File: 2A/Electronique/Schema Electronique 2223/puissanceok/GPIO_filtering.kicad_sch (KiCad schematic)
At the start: 4 parts, among them J201 Conn_01x02

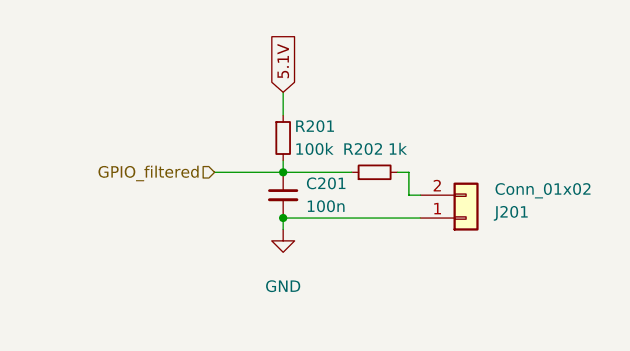
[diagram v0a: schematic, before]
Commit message: update schematic
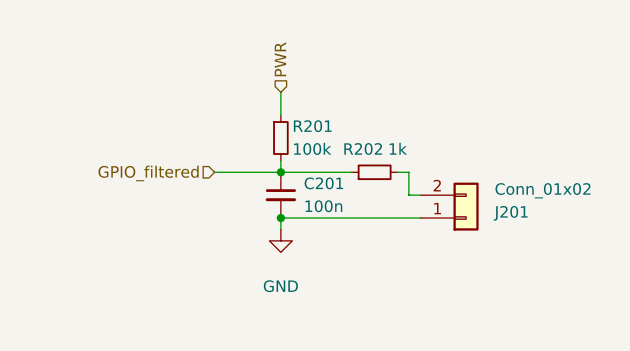
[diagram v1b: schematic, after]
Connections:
- net 5.1V renamed PWR
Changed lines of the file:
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@@
 (kicad_sch (version 20230121) (generator eeschema)
   (paper "A4")
-  (junction (at 122.174 81.28) (diameter 0) (color 0 0 0 0)
-  )
-  (junction (at 122.174 86.36) (diameter 0) (color 0 0 0 0)
-  )
-  (wire (pts (xy 122.174 87.63) (xy 122.174 86.36))
+  (junction (at 121.92 81.28) (diameter 0) (color 0 0 0 0)
+  )
+  (junction (at 121.92 86.36) (diameter 0) (color 0 0 0 0)
+  )
+  (wire (pts (xy 121.92 87.63) (xy 121.92 86.36))
+    (stroke (width 0) (type default))
+  )
+  (wire (pts (xy 121.92 72.39) (xy 121.92 74.93))
     (stroke (width 0) (type default))
   )
@@
     (stroke (width 0) (type default))
   )
-  (wire (pts (xy 122.174 72.39) (xy 122.174 74.93))
-    (stroke (width 0) (type default))
-  )
   (wire (pts (xy 136.144 83.82) (xy 137.414 83.82))
     (stroke (width 0) (type default))
   )
-  (wire (pts (xy 122.174 81.28) (xy 114.554 81.28))
+  (wire (pts (xy 121.92 80.01) (xy 121.92 81.28))
+    (stroke (width 0) (type default))
+  )
+  (wire (pts (xy 121.92 81.28) (xy 129.794 81.28))
     (stroke (width 0) (type default))
   )
@@
     (stroke (width 0) (type default))
   )
-  (wire (pts (xy 122.174 80.01) (xy 122.174 81.28))
-    (stroke (width 0) (type default))
-  )
-  (wire (pts (xy 137.414 86.36) (xy 122.174 86.36))
-    (stroke (width 0) (type default))
-  )
-  (wire (pts (xy 122.174 81.28) (xy 129.794 81.28))
-    (stroke (width 0) (type default))
-  )
-  (global_label "5.1V" (shape input) (at 122.174 72.39 90) (fields_autoplaced)
+  (wire (pts (xy 121.92 86.36) (xy 137.414 86.36))
+    (stroke (width 0) (type default))
+  )
+  (wire (pts (xy 114.554 81.28) (xy 121.92 81.28))
+    (stroke (width 0) (type default))
+  )
+  (hierarchical_label "PWR" (shape input) (at 121.92 72.39 90) (fields_autoplaced)
     (effects (font (size 1.27 1.27)) (justify left))
-    (property "Intersheetrefs" "${INTERSHEET_REFS}" (at 122.174 65.2924 90)
-      (effects (font (size 1.27 1.27)) (justify left) hide)
-    )
   )
   (hierarchical_label "GPIO_filtered" (shape input) (at 114.554 81.28 180) (fields_autoplaced)
     (effects (font (size 1.27 1.27)) (justify right))
   )
-  (symbol (lib_id "Device:R_Small") (at 122.174 77.47 0) (unit 1)
+  (symbol (lib_id "Device:R_Small") (at 121.92 77.47 0) (unit 1)
     (in_bom yes) (on_board yes) (dnp no)
-    (property "Reference" "R201" (at 123.444 76.2 0)
-      (effects (font (size 1.27 1.27)) (justify left))
-    )
-    (property "Value" "100k" (at 123.444 78.74 0)
-      (effects (font (size 1.27 1.27)) (justify left))
-    )
-    (property "Footprint" "Resistor_SMD:R_0402_1005Metric" (at 122.174 77.47 0)
-      (effects (font (size 1.27 1.27)) hide)
-    )
-    (property "Datasheet" "~" (at 122.174 77.47 0)
+    (property "Reference" "R201" (at 123.19 76.2 0)
+      (effects (font (size 1.27 1.27)) (justify left))
+    )
+    (property "Value" "100k" (at 123.19 78.74 0)
+      (effects (font (size 1.27 1.27)) (justify left))
+    )
+    (property "Footprint" "Resistor_SMD:R_0402_1005Metric" (at 121.92 77.47 0)
+      (effects (font (size 1.27 1.27)) hide)
+    )
+    (property "Datasheet" "~" (at 121.92 77.47 0)
       (effects (font (size 1.27 1.27)) hide)
     )
@@
     )
   )
-  (symbol (lib_id "power:GND") (at 122.174 87.63 0) (unit 1)
+  (symbol (lib_id "power:GND") (at 121.92 87.63 0) (unit 1)
     (in_bom yes) (on_board yes) (dnp no)
-    (property "Reference" "#PWR0201" (at 122.174 93.98 0)
-      (effects (font (size 1.27 1.27)) hide)
-    )
-    (property "Value" "GND" (at 122.174 93.98 0)
+    (property "Reference" "#PWR0201" (at 121.92 93.98 0)
+      (effects (font (size 1.27 1.27)) hide)
+    )
+    (property "Value" "GND" (at 121.92 93.98 0)
       (effects (font (size 1.27 1.27)))
     )
-    (property "Footprint" "" (at 122.174 87.63 0)
-      (effects (font (size 1.27 1.27)) hide)
-    )
-    (property "Datasheet" "" (at 122.174 87.63 0)
+    (property "Footprint" "" (at 121.92 87.63 0)
+      (effects (font (size 1.27 1.27)) hide)
+    )
+    (property "Datasheet" "" (at 121.92 87.63 0)
       (effects (font (size 1.27 1.27)) hide)
     )
@@
     )
   )
-  (symbol (lib_id "Device:C_Small") (at 122.174 83.82 0) (unit 1)
+  (symbol (lib_id "Device:C_Small") (at 121.92 83.82 0) (unit 1)
     (in_bom yes) (on_board yes) (dnp no) (fields_autoplaced)
-    (property "Reference" "C201" (at 124.714 82.5563 0)
-      (effects (font (size 1.27 1.27)) (justify left))
-    )
-    (property "Value" "100n" (at 124.714 85.0963 0)
-      (effects (font (size 1.27 1.27)) (justify left))
-    )
-    (property "Footprint" "Capacitor_SMD:C_0402_1005Metric" (at 122.174 83.82 0)
-      (effects (font (size 1.27 1.27)) hide)
-    )
-    (property "Datasheet" "~" (at 122.174 83.82 0)
-      (effects (font (size 1.27 1.27)) hide)
-    )
+    (property "Reference" "C201" (at 124.46 82.5563 0)
+      (effects (font (size 1.27 1.27)) (justify left))
+    )
+    (property "Value" "100n" (at 124.46 85.0963 0)
+      (effects (font (size 1.27 1.27)) (justify left))
+    )
+    (property "Footprint" "Capacitor_SMD:C_0402_1005Metric" (at 121.92 83.82 0)
+      (effects (font (size 1.27 1.27)) hide)
+    )
+    (property "Datasheet" "~" (at 121.92 83.82 0)
+      (effects (font (size 1.27 1.27)) hide)
+    )

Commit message: update schematic
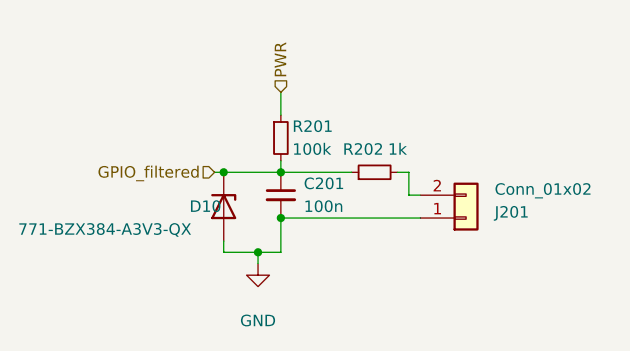
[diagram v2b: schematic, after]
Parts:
- added D10: 771-BZX384-A3V3-QX, Diode_SMD:D_SOD-323, symbol Diode:BZX384xxxx
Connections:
- net GND: now also D10.2 (A)
- net GPIO_filtered: now also D10.1 (K)
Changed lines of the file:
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@@
 (kicad_sch (version 20230121) (generator eeschema)
   (paper "A4")
+  (junction (at 115.57 81.28) (diameter 0) (color 0 0 0 0)
+  )
   (junction (at 121.92 81.28) (diameter 0) (color 0 0 0 0)
   )
   (junction (at 121.92 86.36) (diameter 0) (color 0 0 0 0)
   )
-  (wire (pts (xy 121.92 87.63) (xy 121.92 86.36))
+  (junction (at 119.38 90.17) (diameter 0) (color 0 0 0 0)
+  )
+  (wire (pts (xy 119.38 91.44) (xy 119.38 90.17))
     (stroke (width 0) (type default))
   )
@@
     (stroke (width 0) (type default))
   )
+  (wire (pts (xy 121.92 90.17) (xy 121.92 86.36))
+    (stroke (width 0) (type default))
+  )
   (wire (pts (xy 136.144 83.82) (xy 137.414 83.82))
     (stroke (width 0) (type default))
@@
     (stroke (width 0) (type default))
   )
+  (wire (pts (xy 115.57 81.28) (xy 121.92 81.28))
+    (stroke (width 0) (type default))
+  )
   (wire (pts (xy 121.92 81.28) (xy 129.794 81.28))
     (stroke (width 0) (type default))
@@
     (stroke (width 0) (type default))
   )
+  (wire (pts (xy 119.38 90.17) (xy 121.92 90.17))
+    (stroke (width 0) (type default))
+  )
+  (wire (pts (xy 115.57 88.9) (xy 115.57 90.17))
+    (stroke (width 0) (type default))
+  )
+  (wire (pts (xy 115.57 90.17) (xy 119.38 90.17))
+    (stroke (width 0) (type default))
+  )
   (wire (pts (xy 121.92 86.36) (xy 137.414 86.36))
     (stroke (width 0) (type default))
   )
-  (wire (pts (xy 114.554 81.28) (xy 121.92 81.28))
+  (wire (pts (xy 114.554 81.28) (xy 115.57 81.28))
     (stroke (width 0) (type default))
   )
@@
     )
   )
-  (symbol (lib_id "power:GND") (at 121.92 87.63 0) (unit 1)
-    (in_bom yes) (on_board yes) (dnp no)
-    (property "Reference" "#PWR0201" (at 121.92 93.98 0)
-      (effects (font (size 1.27 1.27)) hide)
-    )
-    (property "Value" "GND" (at 121.92 93.98 0)
+  (symbol (lib_id "Diode:BZX384xxxx") (at 115.57 85.09 270) (unit 1)
+    (in_bom yes) (on_board yes) (dnp no)
+    (property "Reference" "D10" (at 111.76 85.09 90)
+      (effects (font (size 1.27 1.27)) (justify left))
+    )
+    (property "Value" "771-BZX384-A3V3-QX" (at 92.71 87.63 90)
+      (effects (font (size 1.27 1.27)) (justify left))
+    )
+    (property "Footprint" "Diode_SMD:D_SOD-323" (at 111.125 85.09 0)
+      (effects (font (size 1.27 1.27)) hide)
+    )
+    (property "Datasheet" "https://www.mouser.fr/datasheet/2/916/BZX384_Q_SER-2721638.pdf" (at 115.57 85.09 0)
+      (effects (font (size 1.27 1.27)) hide)
+    )
+    (property "Mouser Part Number" "771-BZX384-A3V3-QX" (at 115.57 85.09 90)
+      (effects (font (size 1.27 1.27)) hide)
+    )
+    (pin "2")
+    (pin "1")
+    (instances
+      (project "puissanceok"
+        (path "/50648b18-b1a7-4d76-a5dd-1fad5f3e825e/9b22c488-baa3-42ae-9ef5-b083dc19096a"
+          (reference "D10") (unit 1)
+        )
+        (path "/50648b18-b1a7-4d76-a5dd-1fad5f3e825e/ae22de61-0699-445c-b49e-1232b8ae9dd6"
+          (reference "D11") (unit 1)
+        )
+        (path "/50648b18-b1a7-4d76-a5dd-1fad5f3e825e/991e50e5-567d-4a30-9947-41feef9d79c1"
+          (reference "D12") (unit 1)
+        )
+        (path "/50648b18-b1a7-4d76-a5dd-1fad5f3e825e/461af59c-9ba2-44c6-95d1-ce4131c667f6"
+          (reference "D13") (unit 1)
+        )
+      )
+    )
+  )
+  (symbol (lib_id "power:GND") (at 119.38 91.44 0) (unit 1)
+    (in_bom yes) (on_board yes) (dnp no)
+    (property "Reference" "#PWR0201" (at 119.38 97.79 0)
+      (effects (font (size 1.27 1.27)) hide)
+    )
+    (property "Value" "GND" (at 119.38 97.79 0)
       (effects (font (size 1.27 1.27)))
     )
-    (property "Footprint" "" (at 121.92 87.63 0)
-      (effects (font (size 1.27 1.27)) hide)
-    )
-    (property "Datasheet" "" (at 121.92 87.63 0)
-      (effects (font (size 1.27 1.27)) hide)
-    )
+    (property "Footprint" "" (at 119.38 91.44 0)
+      (effects (font (size 1.27 1.27)) hide)
+    )
+    (property "Datasheet" "" (at 119.38 91.44 0)
+      (effects (font (size 1.27 1.27)) hide)
+    )

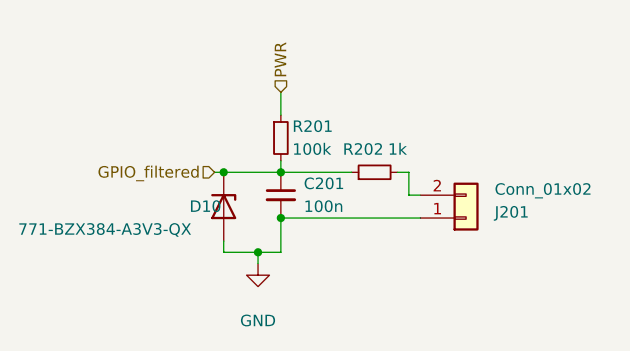
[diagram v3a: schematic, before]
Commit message: suppression diode et changement des feuille hiérarchique
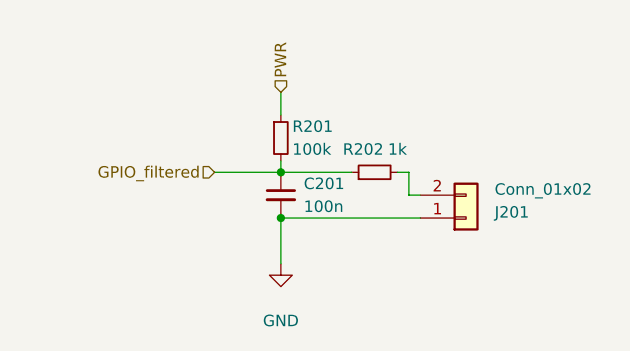
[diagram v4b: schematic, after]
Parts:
- removed D10: 771-BZX384-A3V3-QX, Diode_SMD:D_SOD-323, symbol Diode:BZX384xxxx
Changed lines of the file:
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@@
 (kicad_sch (version 20230121) (generator eeschema)
   (paper "A4")
-  (junction (at 115.57 81.28) (diameter 0) (color 0 0 0 0)
-  )
   (junction (at 121.92 81.28) (diameter 0) (color 0 0 0 0)
   )
   (junction (at 121.92 86.36) (diameter 0) (color 0 0 0 0)
-  )
-  (junction (at 119.38 90.17) (diameter 0) (color 0 0 0 0)
-  )
-  (wire (pts (xy 119.38 91.44) (xy 119.38 90.17))
-    (stroke (width 0) (type default))
   )
   (wire (pts (xy 121.92 72.39) (xy 121.92 74.93))
@@
     (stroke (width 0) (type default))
   )
-  (wire (pts (xy 121.92 90.17) (xy 121.92 86.36))
+  (wire (pts (xy 121.92 86.36) (xy 121.92 91.44))
     (stroke (width 0) (type default))
   )
@@
     (stroke (width 0) (type default))
   )
-  (wire (pts (xy 115.57 81.28) (xy 121.92 81.28))
+  (wire (pts (xy 114.554 81.28) (xy 121.92 81.28))
     (stroke (width 0) (type default))
   )
@@
     (stroke (width 0) (type default))
   )
-  (wire (pts (xy 119.38 90.17) (xy 121.92 90.17))
-    (stroke (width 0) (type default))
-  )
-  (wire (pts (xy 115.57 88.9) (xy 115.57 90.17))
-    (stroke (width 0) (type default))
-  )
-  (wire (pts (xy 115.57 90.17) (xy 119.38 90.17))
-    (stroke (width 0) (type default))
-  )
   (wire (pts (xy 121.92 86.36) (xy 137.414 86.36))
-    (stroke (width 0) (type default))
-  )
-  (wire (pts (xy 114.554 81.28) (xy 115.57 81.28))
     (stroke (width 0) (type default))
   )
@@
     )
   )
-  (symbol (lib_id "Diode:BZX384xxxx") (at 115.57 85.09 270) (unit 1)
+  (symbol (lib_id "power:GND") (at 121.92 91.44 0) (unit 1)
     (in_bom yes) (on_board yes) (dnp no)
-    (property "Reference" "D10" (at 111.76 85.09 90)
-      (effects (font (size 1.27 1.27)) (justify left))
-    )
-    (property "Value" "771-BZX384-A3V3-QX" (at 92.71 87.63 90)
-      (effects (font (size 1.27 1.27)) (justify left))
-    )
-    (property "Footprint" "Diode_SMD:D_SOD-323" (at 111.125 85.09 0)
+    (property "Reference" "#PWR0201" (at 121.92 97.79 0)
       (effects (font (size 1.27 1.27)) hide)
     )
-    (property "Datasheet" "https://www.mouser.fr/datasheet/2/916/BZX384_Q_SER-2721638.pdf" (at 115.57 85.09 0)
+    (property "Value" "GND" (at 121.92 97.79 0)
+      (effects (font (size 1.27 1.27)))
+    )
+    (property "Footprint" "" (at 121.92 91.44 0)
       (effects (font (size 1.27 1.27)) hide)
     )
-    (property "Mouser Part Number" "771-BZX384-A3V3-QX" (at 115.57 85.09 90)
+    (property "Datasheet" "" (at 121.92 91.44 0)
       (effects (font (size 1.27 1.27)) hide)
     )
-    (pin "1")
-    (pin "2")
-    (instances
-      (project "puissanceok"
-        (path "/50648b18-b1a7-4d76-a5dd-1fad5f3e825e/9b22c488-baa3-42ae-9ef5-b083dc19096a"
-          (reference "D10") (unit 1)
-        )
-        (path "/50648b18-b1a7-4d76-a5dd-1fad5f3e825e/ae22de61-0699-445c-b49e-1232b8ae9dd6"
-          (reference "D11") (unit 1)
-        )
-        (path "/50648b18-b1a7-4d76-a5dd-1fad5f3e825e/991e50e5-567d-4a30-9947-41feef9d79c1"
-          (reference "D12") (unit 1)
-        )
-        (path "/50648b18-b1a7-4d76-a5dd-1fad5f3e825e/461af59c-9ba2-44c6-95d1-ce4131c667f6"
-          (reference "D13") (unit 1)
-        )
-      )
-    )
-  )
-  (symbol (lib_id "power:GND") (at 119.38 91.44 0) (unit 1)
-    (in_bom yes) (on_board yes) (dnp no)
-    (property "Reference" "#PWR0201" (at 119.38 97.79 0)
-      (effects (font (size 1.27 1.27)) hide)
-    )
-    (property "Value" "GND" (at 119.38 97.79 0)
-      (effects (font (size 1.27 1.27)))
-    )
-    (property "Footprint" "" (at 119.38 91.44 0)
-      (effects (font (size 1.27 1.27)) hide)
-    )
-    (property "Datasheet" "" (at 119.38 91.44 0)
-      (effects (font (size 1.27 1.27)) hide)
-    )

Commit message: update schematic
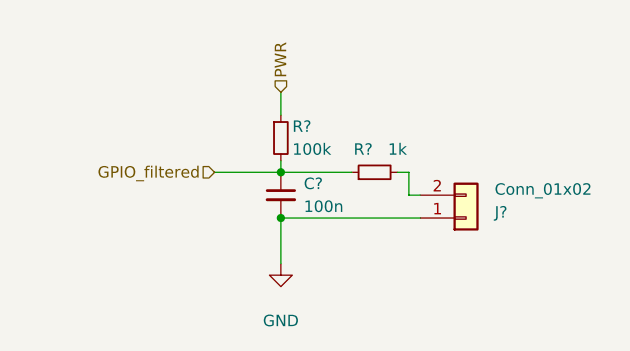
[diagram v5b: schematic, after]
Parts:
- renumbered C201 to C?, J201 to J?, R201 to R?, R202 to R?

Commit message: debut assignation empreintes
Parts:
- C?: footprint Capacitor_SMD:C_0402_1005Metric -> Capacitor_SMD:C_0603_1608Metric_Pad1.08x0.95mm_HandSolder
- R? (x2): footprint Resistor_SMD:R_0402_1005Metric -> Resistor_SMD:R_0603_1608Metric_Pad0.98x0.95mm_HandSolder
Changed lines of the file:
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@@
       (effects (font (size 1.27 1.27)) (justify left))
     )
-    (property "Footprint" "Resistor_SMD:R_0402_1005Metric" (at 121.92 77.47 0)
+    (property "Footprint" "Resistor_SMD:R_0603_1608Metric_Pad0.98x0.95mm_HandSolder" (at 121.92 77.47 0)
       (effects (font (size 1.27 1.27)) hide)
     )
@@
       (effects (font (size 1.27 1.27)))
     )
-    (property "Footprint" "Resistor_SMD:R_0402_1005Metric" (at 132.334 81.28 0)
+    (property "Footprint" "Resistor_SMD:R_0603_1608Metric_Pad0.98x0.95mm_HandSolder" (at 132.334 81.28 0)
       (effects (font (size 1.27 1.27)) hide)
     )
@@
       (effects (font (size 1.27 1.27)) (justify left))
     )
-    (property "Footprint" "Capacitor_SMD:C_0402_1005Metric" (at 121.92 83.82 0)
+    (property "Footprint" "Capacitor_SMD:C_0603_1608Metric_Pad1.08x0.95mm_HandSolder" (at 121.92 83.82 0)
       (effects (font (size 1.27 1.27)) hide)
     )

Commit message: update pcd
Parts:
- C?: footprint Capacitor_SMD:C_0603_1608Metric_Pad1.08x0.95mm_HandSolder -> Capacitor_SMD:C_0402_1005Metric
- J?: footprint (none) -> Connector_JST:JST_XH_B2B-XH-A_1x02_P2.50mm_Vertical
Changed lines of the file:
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@@
       (project "puissanceok"
         (path "/50648b18-b1a7-4d76-a5dd-1fad5f3e825e/9b22c488-baa3-42ae-9ef5-b083dc19096a"
-          (reference "#PWR030") (unit 1)
+          (reference "#PWR032") (unit 1)
         )
         (path "/50648b18-b1a7-4d76-a5dd-1fad5f3e825e/ae22de61-0699-445c-b49e-1232b8ae9dd6"
-          (reference "#PWR036") (unit 1)
+          (reference "#PWR038") (unit 1)
         )
         (path "/50648b18-b1a7-4d76-a5dd-1fad5f3e825e/991e50e5-567d-4a30-9947-41feef9d79c1"
-          (reference "#PWR037") (unit 1)
+          (reference "#PWR039") (unit 1)
         )
         (path "/50648b18-b1a7-4d76-a5dd-1fad5f3e825e/461af59c-9ba2-44c6-95d1-ce4131c667f6"
-          (reference "#PWR043") (unit 1)
+          (reference "#PWR045") (unit 1)
         )
       )
@@
       (effects (font (size 1.27 1.27)) (justify left))
     )
-    (property "Footprint" "Capacitor_SMD:C_0603_1608Metric_Pad1.08x0.95mm_HandSolder" (at 121.92 83.82 0)
+    (property "Footprint" "Capacitor_SMD:C_0402_1005Metric" (at 121.92 83.82 0)
       (effects (font (size 1.27 1.27)) hide)
     )
@@
       (effects (font (size 1.27 1.27)) (justify left))
     )
-    (property "Footprint" "" (at 142.494 86.36 0)
+    (property "Footprint" "Connector_JST:JST_XH_B2B-XH-A_1x02_P2.50mm_Vertical" (at 142.494 86.36 0)
       (effects (font (size 1.27 1.27)) hide)
     )
@@
       (project "puissanceok"
         (path "/50648b18-b1a7-4d76-a5dd-1fad5f3e825e/9b22c488-baa3-42ae-9ef5-b083dc19096a"
-          (reference "J13") (unit 1)
+          (reference "J16") (unit 1)
         )
         (path "/50648b18-b1a7-4d76-a5dd-1fad5f3e825e/ae22de61-0699-445c-b49e-1232b8ae9dd6"
-          (reference "J14") (unit 1)
+          (reference "J17") (unit 1)
         )
         (path "/50648b18-b1a7-4d76-a5dd-1fad5f3e825e/991e50e5-567d-4a30-9947-41feef9d79c1"
-          (reference "J15") (unit 1)
+          (reference "J18") (unit 1)
         )
         (path "/50648b18-b1a7-4d76-a5dd-1fad5f3e825e/461af59c-9ba2-44c6-95d1-ce4131c667f6"
-          (reference "J16") (unit 1)
+          (reference "J19") (unit 1)
         )
       )

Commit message: finalize schematic + footprints
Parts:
- J?: value Conn_01x02 -> Conn_FDC
- R? (x2): footprint Resistor_SMD:R_0603_1608Metric_Pad0.98x0.95mm_HandSolder -> Resistor_SMD:R_0402_1005Metric
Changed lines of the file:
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@@
       (effects (font (size 1.27 1.27)) (justify left))
     )
-    (property "Footprint" "Resistor_SMD:R_0603_1608Metric_Pad0.98x0.95mm_HandSolder" (at 121.92 77.47 0)
+    (property "Footprint" "Resistor_SMD:R_0402_1005Metric" (at 121.92 77.47 0)
       (effects (font (size 1.27 1.27)) hide)
     )
@@
       (effects (font (size 1.27 1.27)))
     )
-    (property "Footprint" "Resistor_SMD:R_0603_1608Metric_Pad0.98x0.95mm_HandSolder" (at 132.334 81.28 0)
+    (property "Footprint" "Resistor_SMD:R_0402_1005Metric" (at 132.334 81.28 0)
       (effects (font (size 1.27 1.27)) hide)
     )
@@
       (effects (font (size 1.27 1.27)) (justify left))
     )
-    (property "Value" "Conn_01x02" (at 145.669 83.185 0)
-      (effects (font (size 1.27 1.27)) (justify left))
-    )
+    (property "Value" "Conn_FDC" (at 145.669 83.185 0)
+      (effects (font (size 1.27 1.27)) (justify left))
+    )
